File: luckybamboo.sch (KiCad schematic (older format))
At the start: 153 parts, among them J1 NEIGHBOR1, J10 TEST_2P, J11 TEST_2P, J12 TEST_2P, J13 TEST_2P, J14 TEST_2P, J15 TEST_2P, J16 TEST_2P, J17 Conn_Coaxial, J18 Conn_Coaxial, J19 TEST_2P, J2 NEIGHBOR2, J20 TEST_2P, J21 TEST_2P, J22 TEST_2P, J23 TEST_2P, J24 TEST_2P, J25 TEST_2P, J26 TEST_2P, J27 TEST_2P, J28 TEST_2P, J29 TEST_2P, J3 Conn_01x08, J30 TEST_2P, J31 TEST_2P, J32 TEST_2P, J33 TEST_2P, J4 Conn_01x08, J5 Conn_01x08, J6 Conn_01x08, J7 BONUS_ROW, J8 TEST_2P, J9 TEST_2P, U1 ADF7242, U10 ADF7242_balun, U11 ADF7242_balun, U12 HHM2293A1, U13 BGA7H1N6, U14 ADF7242_balun, U15 ADF7242_balun, U16 ADF7242_balun, U17 ADF7242_balun, U2 ADF7242, U3 ADF7242, U4 ADF7242, U5 SKY13322, U6 HHM2293A1, U7 HHM2293A1, U8 ADF7242_balun, U9 ADF7242_balun, X1 XTAL4PIN, X2 XTAL4PIN, X3 XTAL4PIN, X4 XTAL4PIN

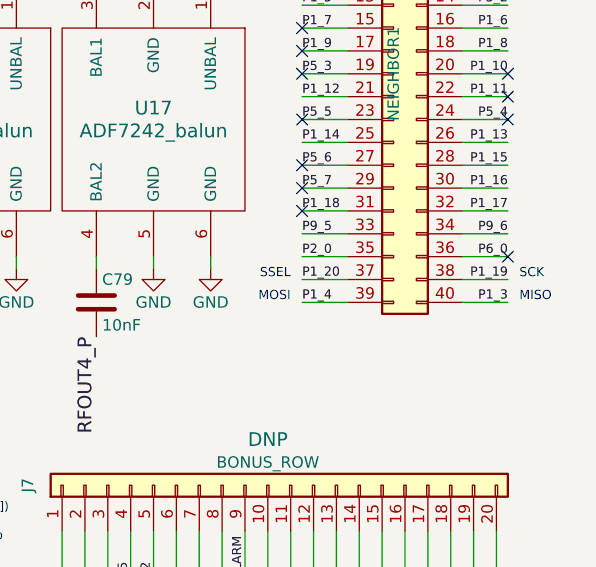
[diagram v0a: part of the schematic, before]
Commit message: adopt OSHWA convention for SPI signal names https://www.oshwa.org/a-resolution-to-redefine-spi-signal-names
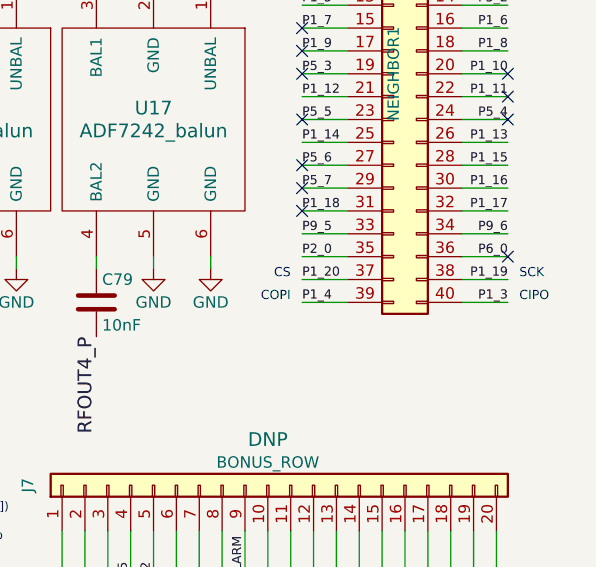
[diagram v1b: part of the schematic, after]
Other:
- note added: "CIPO"
- note added: "COPI"
- note added: "CS"
- note removed: "MISO"
- note removed: "MOSI"
- note removed: "SSEL"
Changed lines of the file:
@@
 P2_0
 Text Notes 16250 6200 0    40   ~ 0
-MISO
+CIPO
 Text Notes 15250 6200 2    40   ~ 0
-MOSI
+COPI
 Text Notes 16250 6100 0    40   ~ 0
 SCK
 Text Notes 15250 6100 2    40   ~ 0
-SSEL
+CS
 Text Label 16300 3850 2    40   ~ 0
 I2C0_SCL
